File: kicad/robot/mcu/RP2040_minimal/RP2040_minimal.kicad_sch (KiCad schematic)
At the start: 36 parts, among them J2 Conn_01x02, U2 W25Q128JVS, U3 RP2040, U7 SN74AHC125RGYR, Y1 ABLS-12.000MHZ-B4-T

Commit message: Replaced footprint with 2 pad short test point
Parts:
- TP28: footprint TestPoint:TestPoint_2Pads_Pitch2.54mm_Drill0.8mm -> TestPoint:TestPoint_2Pads_Pitch2mm_SMD; now left out of the parts list
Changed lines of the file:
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@@
   )
   (symbol (lib_id "custom_connectors:TestPoint_CurrentShunt") (at 140.97 165.1 180) (unit 1)
-    (in_bom yes) (on_board yes)
+    (in_bom no) (on_board yes)
     (property "Reference" "TP28" (id 0) (at 140.97 161.29 0))
     (property "Value" "SWD" (id 1) (at 140.97 158.75 0))
-    (property "Footprint" "TestPoint:TestPoint_2Pads_Pitch2.54mm_Drill0.8mm" (id 2) (at 140.97 170.18 0)
+    (property "Footprint" "TestPoint:TestPoint_2Pads_Pitch2mm_SMD" (id 2) (at 140.97 170.18 0)
       (effects (font (size 1.27 1.27)) hide)
     )

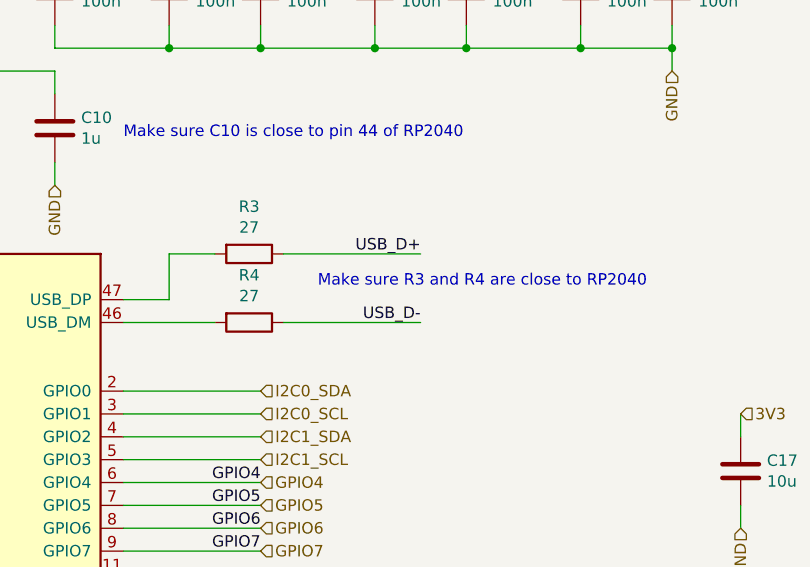
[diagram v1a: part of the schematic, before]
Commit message: Added USB-C Source sheet and connector
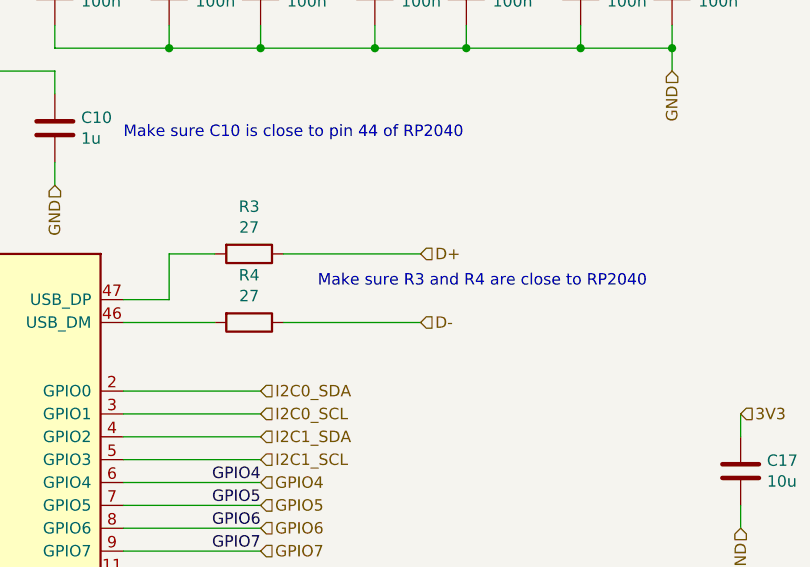
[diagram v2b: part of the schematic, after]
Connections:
- net USB_D+ renamed D+
- net USB_D- renamed D-
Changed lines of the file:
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@@
-    (effects (font (size 1.27 1.27)) (justify right bottom))
-  )
-  (label "USB_D+" (at 264.16 96.52 180)
     (effects (font (size 1.27 1.27)) (justify right bottom))
   )
@@
   )
   (label "XIN" (at 99.06 218.44 180)
-    (effects (font (size 1.27 1.27)) (justify right bottom))
-  )
-  (label "USB_D-" (at 264.16 104.14 180)
     (effects (font (size 1.27 1.27)) (justify right bottom))
   )
@@
     (effects (font (size 1.27 1.27)) (justify right))
   )
+  (hierarchical_label "D-" (shape input) (at 264.16 104.14 0)
+    (effects (font (size 1.27 1.27)) (justify left))
+  )
   (hierarchical_label "I2C1_SCL" (shape input) (at 246.38 119.38 0)
     (effects (font (size 1.27 1.27)) (justify left))
@@
     (effects (font (size 1.27 1.27)) (justify right))
   )
+  (hierarchical_label "D+" (shape input) (at 264.16 96.52 0)
+    (effects (font (size 1.27 1.27)) (justify left))
+  )
   (hierarchical_label "GND" (shape input) (at 86.36 114.3 270)

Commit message: Updated SN74AHC125RGYR_0_0 symbol to include pads
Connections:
- net GND: now also U7.PAD (GND)
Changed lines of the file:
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@@
       (effects (font (size 1.524 1.524)) hide)
     )
+    (pin "PAD")
     (pin "1")
     (pin "10")

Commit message: Changing remaining square pads to rounded squares
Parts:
- TP27: footprint custom_connectors:2.54mm_2pointCurrentTestPoint -> Connector_PinHeader_2.54mm:PinHeader_1x02_P2.54mm_Vertical
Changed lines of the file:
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@@
       (effects (font (size 1.27 1.27)) (justify left))
     )
-    (property "Footprint" "custom_connectors:2.54mm_2pointCurrentTestPoint" (id 2) (at 138.43 177.8 0)
-      (effects (font (size 1.27 1.27)) hide)
+    (property "Footprint" "Connector_PinHeader_2.54mm:PinHeader_1x02_P2.54mm_Vertical" (id 2) (at 138.43 177.8 0)
+      (effects (font (size 0 0)) hide)
     )
     (property "Datasheet" "https://www.digikey.jp/product-detail/en/kycon-inc/SX1100-B/2092-SX1100-B-ND/9990206" (id 3) (at 135.89 177.8 0)

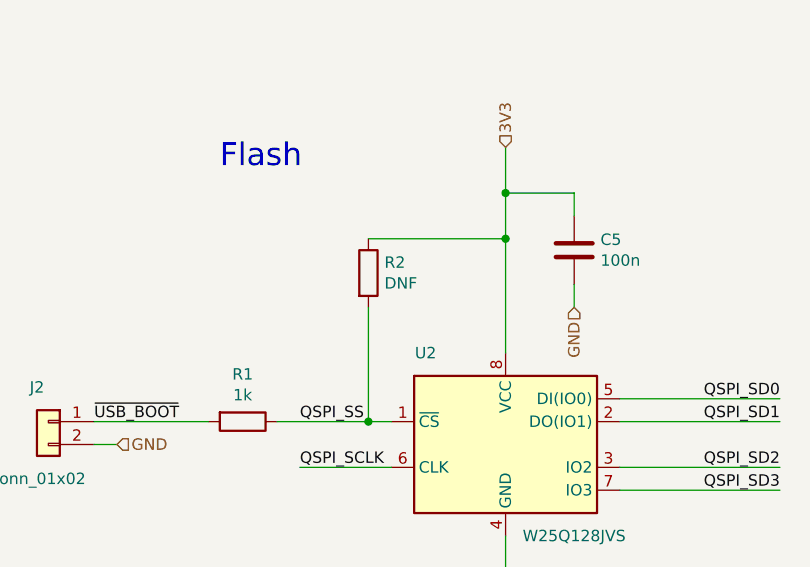
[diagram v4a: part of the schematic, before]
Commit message: Remove some more DNP parts from BOM
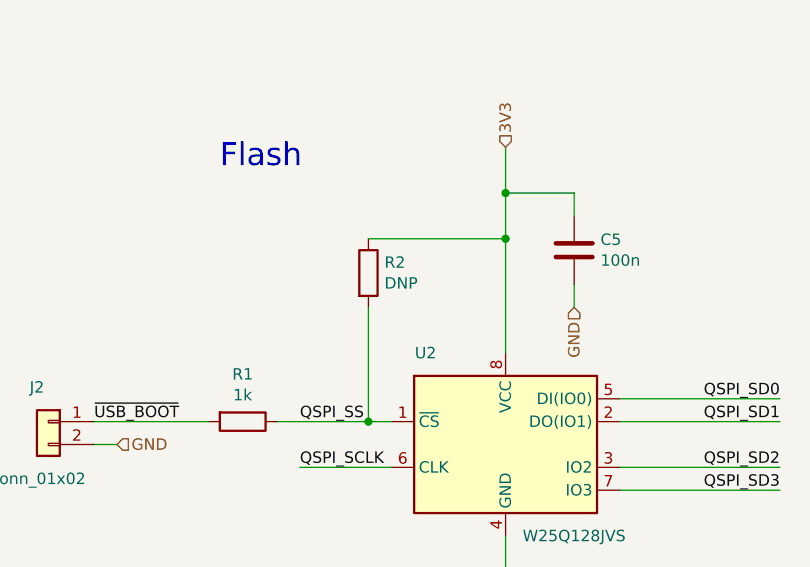
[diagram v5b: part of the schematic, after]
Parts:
- R2: value DNF -> DNP; now left out of the parts list
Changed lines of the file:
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@@
   )
   (symbol (lib_id "Device:R") (at 63.5 110.49 0) (unit 1)
-    (in_bom yes) (on_board yes)
+    (in_bom no) (on_board yes)
     (property "Reference" "R2" (id 0) (at 65.278 109.3216 0)
       (effects (font (size 1.27 1.27)) (justify left))
     )
-    (property "Value" "DNF" (id 1) (at 65.278 111.633 0)
+    (property "Value" "DNP" (id 1) (at 65.278 111.633 0)
       (effects (font (size 1.27 1.27)) (justify left))
     )

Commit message: WARNING Major BOM cleanup
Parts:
- TP27: value SWD -> 2PinHeader
- TP28: value SWD -> TP2PinPads
- TP35: renamed from J2; value Conn_01x02 -> 2PinHeader
- Y1: Manufacturer (none) -> Abracon LLC; Part Number (none) -> ABLS-12.000MHZ-B4-T
- renumbered U7 to Q5
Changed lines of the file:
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@@
+      (effects (font (size 1.27 1.27)) hide)
+    )
+    (property "Manufacturer" "Abracon LLC" (id 4) (at 66.04 224.79 0)
+      (effects (font (size 1.27 1.27)) hide)
+    )
+    (property "Part Number" "ABLS-12.000MHZ-B4-T" (id 5) (at 66.04 224.79 0)
       (effects (font (size 1.27 1.27)) hide)
     )
@@
   (symbol (lib_id "Connector_Generic:Conn_01x02") (at 27.94 127 0) (mirror y) (unit 1)
     (in_bom yes) (on_board yes)
-    (property "Reference" "J2" (id 0) (at 26.67 123.19 0))
-    (property "Value" "Conn_01x02" (id 1) (at 26.67 133.35 0))
+    (property "Reference" "TP35" (id 0) (at 26.67 123.19 0))
+    (property "Value" "2PinHeader" (id 1) (at 26.67 133.35 0))
     (property "Footprint" "Connector_PinHeader_2.54mm:PinHeader_1x02_P2.54mm_Vertical" (id 2) (at 27.94 127 0)
       (effects (font (size 1.27 1.27)) hide)
@@
   (symbol (lib_id "ultralibrarian:SN74AHC125RGYR") (at 292.1 245.11 0) (unit 1)
     (in_bom yes) (on_board yes)
-    (property "Reference" "U7" (id 0) (at 297.18 227.33 0)
+    (property "Reference" "Q5" (id 0) (at 297.18 227.33 0)
       (effects (font (size 1.524 1.524)) (justify left))
     )
@@
     (in_bom no) (on_board yes)
     (property "Reference" "TP28" (id 0) (at 140.97 161.29 0))
-    (property "Value" "SWD" (id 1) (at 140.97 158.75 0))
+    (property "Value" "TP2PinPads" (id 1) (at 140.97 158.75 0))
     (property "Footprint" "TestPoint:TestPoint_2Pads_Pitch2mm_SMD" (id 2) (at 140.97 170.18 0)
       (effects (font (size 1.27 1.27)) hide)
     )
     (property "Datasheet" "https://www.digikey.jp/product-detail/en/kycon-inc/SX1100-B/2092-SX1100-B-ND/9990206" (id 3) (at 140.97 172.72 0)
+      (effects (font (size 1.27 1.27)) hide)
+    )
+    (property "Description" "Run" (id 4) (at 140.97 165.1 0)
       (effects (font (size 1.27 1.27)) hide)
     )
@@
       (effects (font (size 1.27 1.27)) (justify left))
     )
-    (property "Value" "SWD" (id 1) (at 138.43 179.07 90)
+    (property "Value" "2PinHeader" (id 1) (at 138.43 179.07 90)
       (effects (font (size 1.27 1.27)) (justify left))
     )
@@
       (effects (font (size 1.27 1.27)) hide)
     )
-    (property "Description" "2-pin male header" (id 4) (at 143.51 177.8 0)
+    (property "Description" "MCU_SWD" (id 4) (at 143.51 177.8 0)
       (effects (font (size 1.27 1.27)) hide)
     )

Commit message: WARNING more BOM batch edits
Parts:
- Q5: Part Number (none) -> SN74AHC125RGYR
- TP27, TP35: Part Number (none) -> PH1-02-UA
- TP28: Part Number (none) -> N/A
- U2: Part Number (none) -> W25Q128JVS
- U3: Part Number (none) -> RP2040
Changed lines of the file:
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@@
+      (effects (font (size 1.27 1.27)) hide)
+    )
+    (property "Part Number" "RP2040" (id 4) (at 199.39 144.78 0)
       (effects (font (size 1.27 1.27)) hide)
     )
@@
       (effects (font (size 1.27 1.27)) hide)
     )
+    (property "Part Number" "W25Q128JVS" (id 4) (at 78.74 129.54 0)
+      (effects (font (size 1.27 1.27)) hide)
+    )
     (pin "1")
     (pin "2")
@@
       (effects (font (size 1.27 1.27)) hide)
     )
+    (property "Description" "Adam Tech" (id 4) (at 27.94 127 0)
+      (effects (font (size 1.27 1.27)) hide)
+    )
+    (property "Part Number" "PH1-02-UA" (id 5) (at 27.94 127 0)
+      (effects (font (size 1.27 1.27)) hide)
+    )
     (pin "1")
     (pin "2")
@@
     (property "Datasheet" "https://www.ti.com/lit/ds/symlink/sn74ahc125.pdf?ts=1663326066450&ref_url=https%253A%252F%252Fwww.ti.com%252Fproduct%252FSN74AHC125%252Fpart-details%252FSN74AHC125RGYR" (id 3) (at 292.1 245.11 0)
       (effects (font (size 1.524 1.524)) hide)
+    )
+    (property "Part Number" "SN74AHC125RGYR" (id 4) (at 292.1 245.11 0)
+      (effects (font (size 1.27 1.27)) hide)
     )
     (pin "PAD")
@@
       (effects (font (size 1.27 1.27)) hide)
     )
+    (property "Part Number" "N/A" (id 5) (at 140.97 165.1 0)
+      (effects (font (size 1.27 1.27)) hide)
+    )
     (pin "1")
     (pin "2")
@@
       (effects (font (size 1.27 1.27)) hide)
     )
-    (property "Description" "MCU_SWD" (id 4) (at 143.51 177.8 0)
-      (effects (font (size 1.27 1.27)) hide)
-    )
+    (property "Description" "Adam Tech" (id 4) (at 143.51 177.8 0)
+      (effects (font (size 1.27 1.27)) hide)
+    )
+    (property "Part Number" "PH1-02-UA" (id 5) (at 143.51 177.8 0)
+      (effects (font (size 1.27 1.27)) hide)
+    )

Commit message: Added stock counts to parts I have
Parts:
- Q5: Stock (none) -> 50
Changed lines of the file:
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@@
+      (effects (font (size 1.27 1.27)) hide)
+    )
+    (property "Stock" "50" (id 5) (at 292.1 245.11 0)
       (effects (font (size 1.27 1.27)) hide)
     )
